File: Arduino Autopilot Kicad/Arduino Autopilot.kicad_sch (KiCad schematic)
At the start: 28 parts, among them J1 12V_in, J2 to_clock, J3 to_RTC, J4 to_LCD, SW1 SW_Push

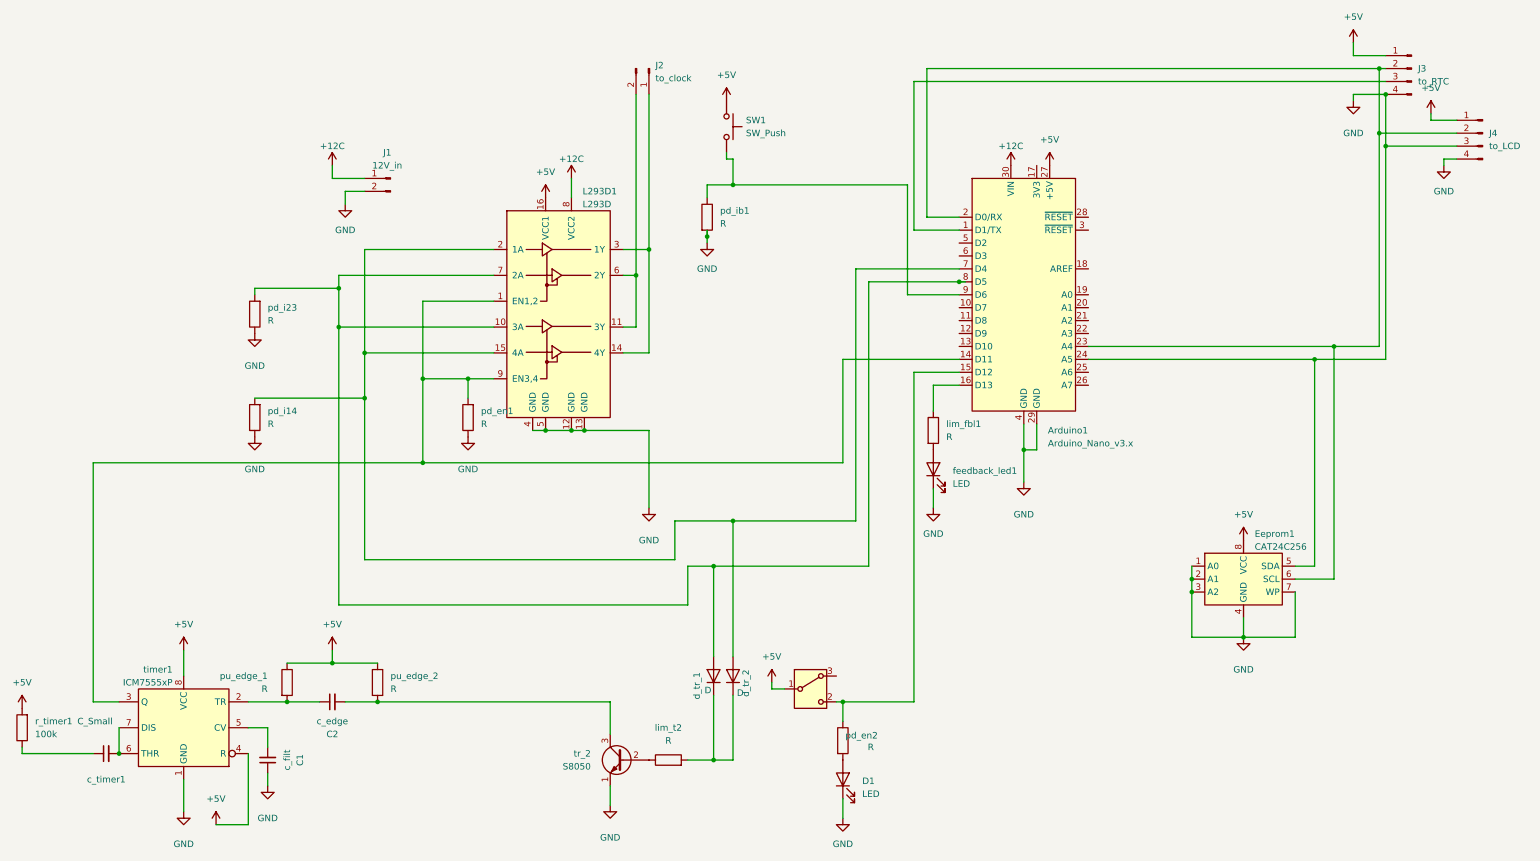
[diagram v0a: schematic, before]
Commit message: updated board circuit, added serial commands parsing, update documentation
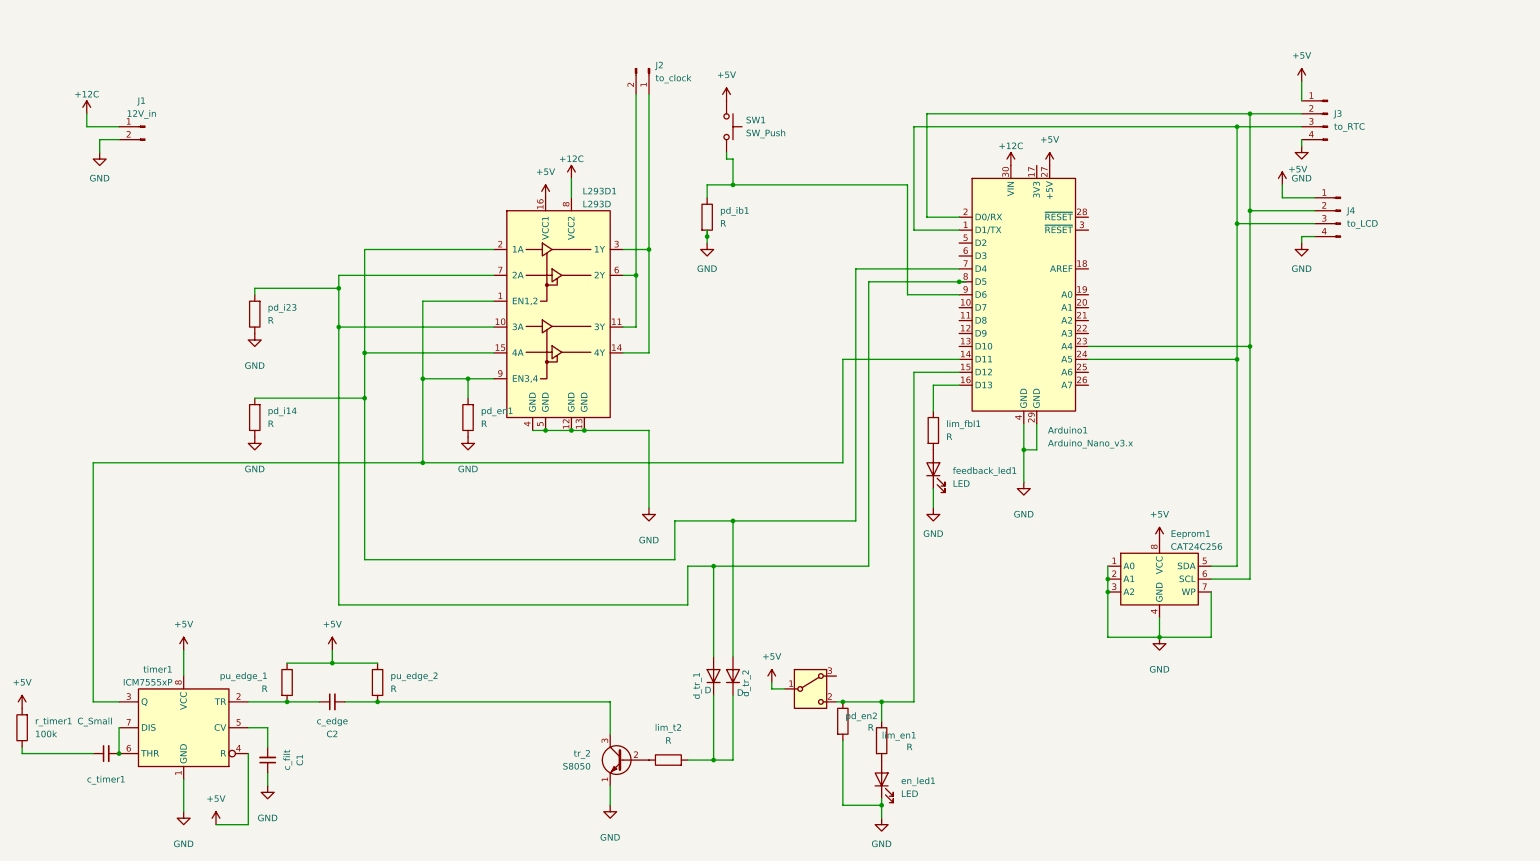
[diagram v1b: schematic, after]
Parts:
- added pd_en2: R, Resistor_THT:R_Axial_DIN0207_L6.3mm_D2.5mm_P7.62mm_Horizontal, symbol Device:R
- renumbered D1 to en_led1, pd_en2 to lim_en1
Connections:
- net GND: now also pd_en2.2; no longer Arduino1.24 (A5), Eeprom1.5 (SDA), J4.3 (Pin_3)
- net at Arduino1.15 (D12), Enableswitch1.2 (C), lim_en1.1: now also pd_en2.1
- net at Arduino1.1 (D1/TX), J3.3 (Pin_3): now also Arduino1.24 (A5), Eeprom1.5 (SDA), J4.3 (Pin_3)
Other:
- moved on the sheet: Eeprom1, J1, J3, J4, en_led1, lim_en1

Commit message: fixed dst management when sending manual inputs, fixed delay capacitor wiring in circuit
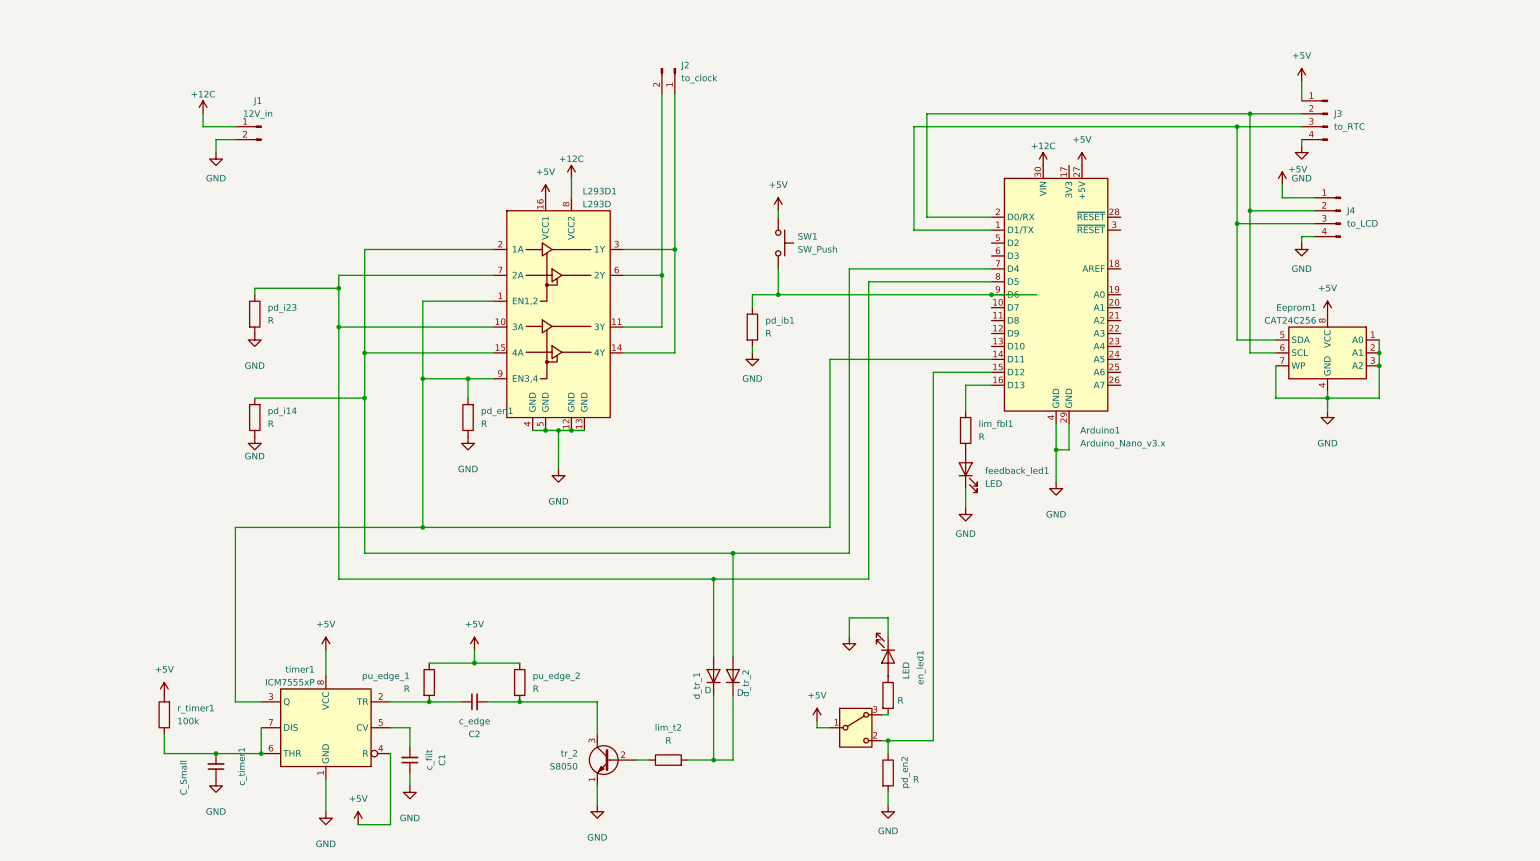
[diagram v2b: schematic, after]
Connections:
- net GND: now also c_timer1.1, pd_i23.2; no longer pd_i23.1
- net at Arduino1.15 (D12), Enableswitch1.2 (C), pd_en2.1: no longer lim_en1.1
- net at Enableswitch1.3 (A): now also lim_en1.2
- net at Arduino1.8 (D5), L293D1.10 (3A), L293D1.7 (2A)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: now also pd_i23.1; no longer pd_i23.2
- net at r_timer1.1: now also c_timer1.2, timer1.6 (THR), timer1.7 (DIS); no longer c_timer1.1
- net at en_led1.2 (A): now also lim_en1.1; no longer lim_en1.2
- net at Arduino1.1 (D1/TX), Eeprom1.5 (SDA), J3.3 (Pin_3)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: no longer Arduino1.24 (A5)
- net at Arduino1.2 (D0/RX), Eeprom1.6 (SCL), J3.2 (Pin_2)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: no longer Arduino1.23 (A4)
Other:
- moved on the sheet: Arduino1, C1, C2, Eeprom1, J1, J2, SW1, c_timer1, feedback_led1, lim_fbl1, pd_en2, pd_i23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

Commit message: updated pin layout, updated circuit and board design
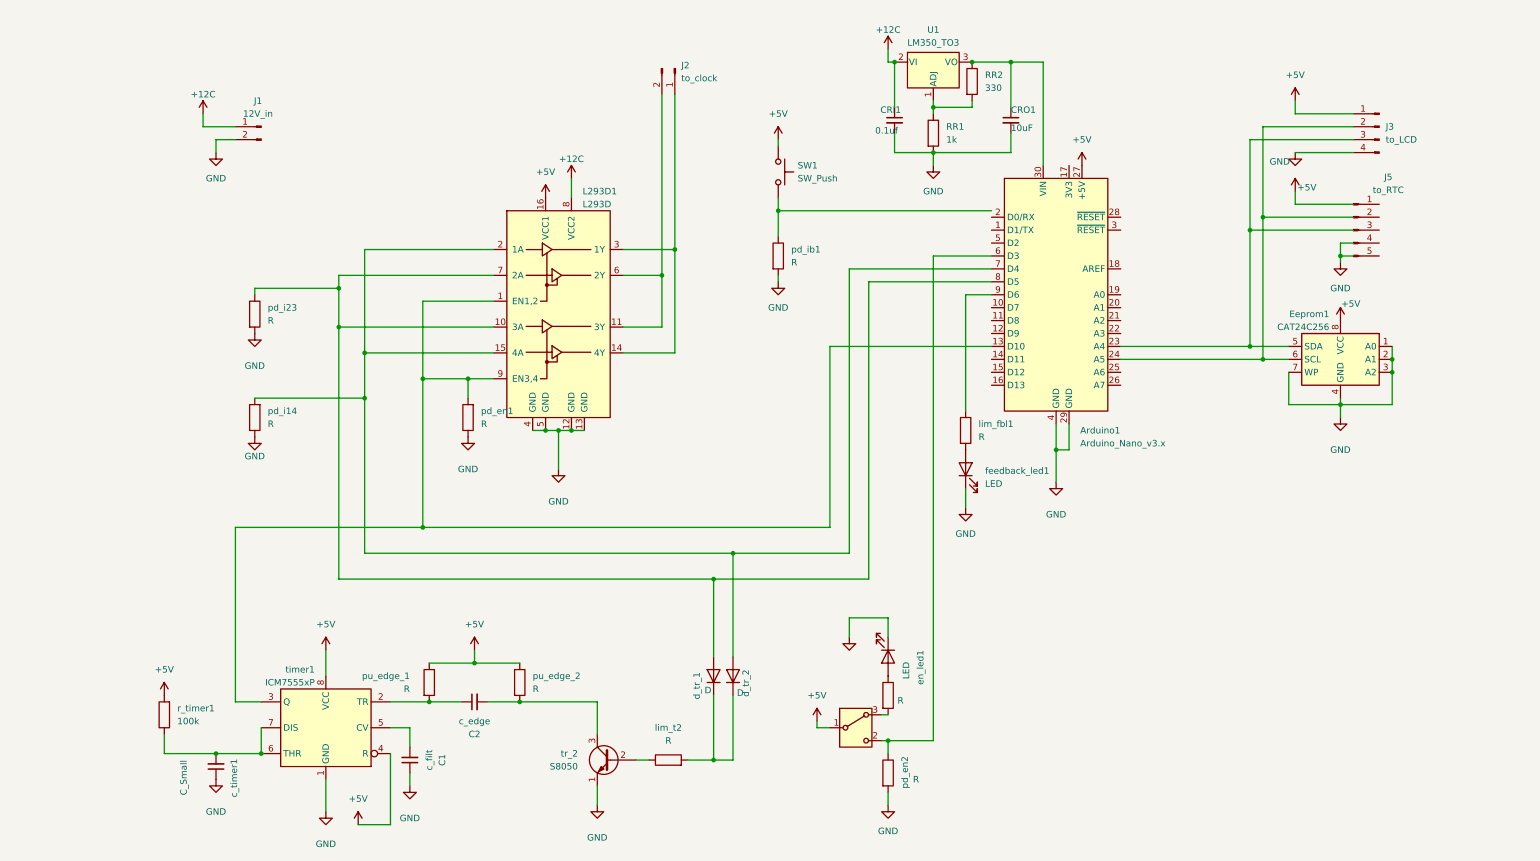
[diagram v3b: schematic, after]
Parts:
- removed J4: to_LCD, Connector_Wire:SolderWire-0.1sqmm_1x04_P3.6mm_D0.4mm_OD1mm, symbol Connector:Conn_01x04_Pin
- added CRI1: 0.1uf, Capacitor_THT:C_Disc_D5.1mm_W3.2mm_P5.00mm, symbol Device:C_Small
- added CRO1: 10uF, Capacitor_THT:C_Disc_D5.1mm_W3.2mm_P5.00mm, symbol Device:C_Small
- added J5: to_RTC, TerminalBlock:TerminalBlock_Xinya_XY308-2.54-5P_1x05_P2.54mm_Horizontal, symbol Connector:Conn_01x05_Pin
- added RR1: 1k, Resistor_THT:R_Axial_DIN0207_L6.3mm_D2.5mm_P7.62mm_Horizontal, symbol Device:R
- added RR2: 330, Resistor_THT:R_Axial_DIN0207_L6.3mm_D2.5mm_P7.62mm_Horizontal, symbol Device:R
- added U1: LM350_TO3, Package_TO_SOT_THT:TO-3PB-3_Vertical, symbol Regulator_Linear:LM350_TO3
- J3: value to_RTC -> to_LCD; footprint Connector_Wire:SolderWire-0.1sqmm_1x04_P3.6mm_D0.4mm_OD1mm -> TerminalBlock:TerminalBlock_Xinya_XY308-2.54-4P_1x04_P2.54mm_Horizontal
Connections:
- net +12C: now also CRI1.1, U1.2 (VI); no longer Arduino1.30 (VIN)
- net GND: now also CRI1.2, CRO1.2, RR1.2
- net at lim_fbl1.1: now also Arduino1.9 (D6); no longer Arduino1.16 (D13)
- net at Enableswitch1.2 (C), pd_en2.1: now also Arduino1.6 (D3); no longer Arduino1.15 (D12)
- net at L293D1.1 (EN1,2), L293D1.9 (EN3,4), pd_en1.2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: now also Arduino1.13 (D10); no longer Arduino1.14 (D11)
- net at Eeprom1.5 (SDA), J3.3 (Pin_3): now also Arduino1.23 (A4); no longer Arduino1.1 (D1/TX)
- net at Eeprom1.6 (SCL), J3.2 (Pin_2): now also Arduino1.24 (A5); no longer Arduino1.2 (D0/RX)
- net at SW1.2, pd_ib1.1: no longer Arduino1.9 (D6)
- new net: Arduino1.30 (VIN), CRO1.1, RR2.1, U1.3 (VO)
- new net: RR1.1, RR2.2, U1.1 (ADJ)
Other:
- moved on the sheet: Eeprom1, J3, SW1, pd_ib1
